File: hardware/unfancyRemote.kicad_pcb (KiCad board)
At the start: 2 copper layers, 27.7 x 59.2 mm, 41 parts, among them J1 Arduino Analog, J2 Arduino Digital, J3 HALL1, J4 HALL2, J5 PPM, J6 VIN, J7 VBAT, J8 Motor, J9 Extra analog 1, Q1 AO3401A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

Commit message: Software v1.0 for rx and tx
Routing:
- net Net-(D6-Pad2): track 0.00 -> 1.99 mm
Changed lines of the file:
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@@
   (segment (start 121.2365 89.662) (end 121.2365 88.2505) (width 0.25) (layer "F.Cu") (net 26))
   (segment (start 121.2365 88.2505) (end 121.603 87.884) (width 0.25) (layer "F.Cu") (net 26))
+  (segment (start 121.603 94.234) (end 121.158 94.679) (width 0.25) (layer "F.Cu") (net 27))
+  (segment (start 121.158 94.679) (end 121.158 95.9335) (width 0.25) (layer "F.Cu") (net 27))
+  (segment (start 121.158 95.9335) (end 121.2365 96.012) (width 0.25) (layer "F.Cu") (net 27))
   (segment (start 123.253 92.057) (end 126.39 88.92) (width 0.25) (layer "F.Cu") (net 28))
   (segment (start 123.253 94.234) (end 123.253 92.057) (width 0.25) (layer "F.Cu") (net 28))

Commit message: Improved transmission stability
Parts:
- added R14: 100K, Resistor_SMD:R_0603_1608Metric, F.Cu at (144.3, 92.7)
- R1: value 220K -> 100K
- moved J7 4.06 mm to (144.3, 89.4)
- moved R12 2.86 mm to (144.3, 86.4)
- moved R13 2.41 mm to (144.3, 83.2)
- turned R1 to 0 degrees
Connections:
- R1 pad 1: BSENSE -> Net-(R1-Pad1)
- R1 pad 2: GND -> BSENSE
- R3 pad 1: BSENSE -> Net-(R1-Pad1)
- SW1 pad 1: BSENSE -> Net-(R1-Pad1)
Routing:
- net Net-(R1-Pad1): track 0.00 -> 23.1 mm, vias 0 -> 2
- net BSENSE: track 28.0 -> 7.62 mm, vias 2 -> 0
- net Net-(J7-Pad1): track 3.43 -> 2.22 mm

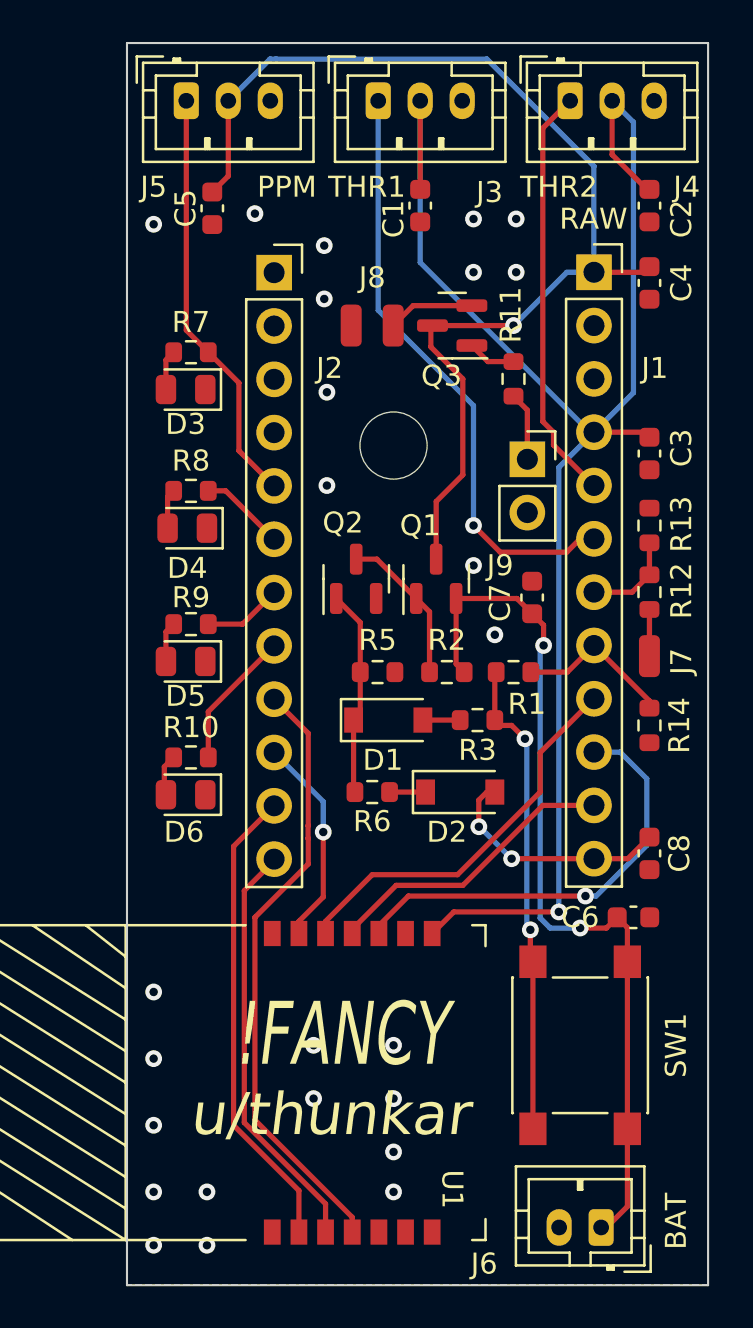
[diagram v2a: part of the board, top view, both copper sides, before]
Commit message: PCB improvements, round version, cal procedure
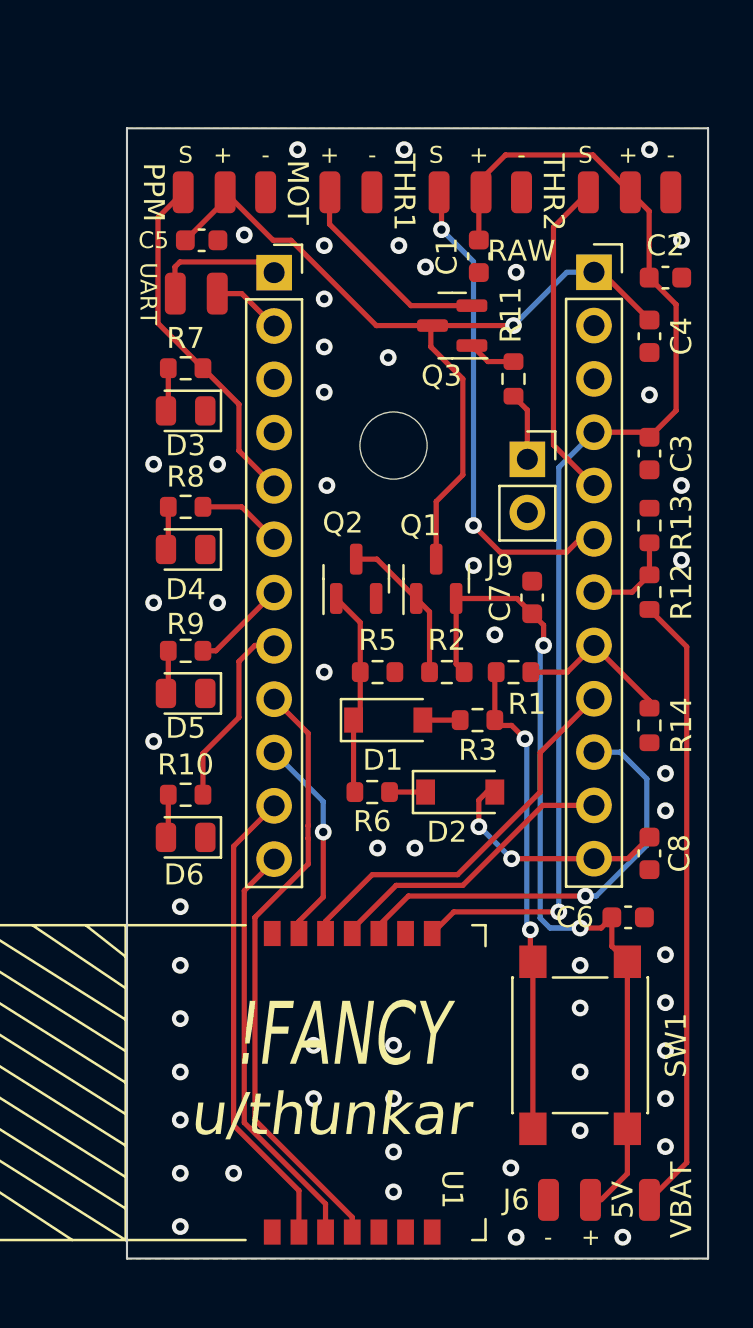
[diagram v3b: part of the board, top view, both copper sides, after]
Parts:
- added J10: UART, unfancyRemote_components:SolderWirePad_1x02_SMD_1x2mm, F.Cu at (122.7, 72.1)
- J3, J4, J5: footprint Connector_JST:JST_PH_B3B-PH-K_1x03_P2.00mm_Vertical -> unfancyRemote_components:SolderWirePad_1x03_SMD_1x2mm
- J6: footprint Connector_JST:JST_PH_B2B-PH-K_1x02_P2.00mm_Vertical -> unfancyRemote_components:SolderWirePad_1x02_SMD_1x2mm
- moved J7 25.9 mm to (144.3, 115.3)
- moved J3 6.48 mm to (136.1, 67.3)
- moved J8 6.43 mm to (130.0, 67.3), turned to 0 degrees
- moved J4 5.16 mm to (143.3, 67.3)
- moved J5 4.70 mm to (124.0, 67.3)
- moved C1 3.69 mm to (136.1, 70.4)
- moved C2 3.51 mm to (145.0, 71.4), turned to 0 degrees
- moved C4 2.54 mm to (144.3, 74.2)
- moved D6 2.03 mm to (122.2, 98.0)
- moved J6 2.00 mm to (140.5, 115.3)
- moved R10 1.80 mm to (122.2, 96.0)
- moved C5 1.61 mm to (122.9, 69.6), turned to 0 degrees
- moved D5 1.52 mm to (122.2, 91.2)
- moved R9 1.30 mm to (122.2, 89.2)
- moved D4 1.02 mm to (122.2, 84.3)
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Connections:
- J2 pad 1: unconnected-(J2-Pad1) -> Net-(J2-Pad1)
- J2 pad 2: unconnected-(J2-Pad2) -> Net-(J2-Pad2)
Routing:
- net Net-(J7-Pad1): track 2.22 -> 29.6 mm
- net +3V3: track 77.5 -> 57.1 mm
- net +5V: track 53.9 -> 40.2 mm
- net Net-(J2-Pad1): track 0.00 -> 6.31 mm
- net Net-(J8-Pad1): track 4.14 -> 9.92 mm
- net HALL1: track 28.6 -> 23.1 mm, vias 1 -> 2
- net HALL2: track 19.9 -> 15.5 mm
- net Net-(J2-Pad2): track 0.00 -> 3.35 mm
- net PPM: track 20.1 -> 16.8 mm
- net L4: track 6.61 -> 9.06 mm
- net 5VRAW: track 42.6 -> 40.9 mm
- net L3: track 3.76 -> 4.54 mm
- net GND: vias 25 -> 55
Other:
- board size 27.7 x 59.2 mm -> 27.7 x 53.8 mm
- board text added: "+"
- board text added: "-"
- board text added: "5V"
- board text added: "MOT"
- board text added: "S"
- board text added: "UART"
- board text added: "VBAT"
- board text removed: "BAT"

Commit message: PCB v2 gerber and bom
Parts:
- moved J9 2.55 mm to (139.0, 82.5), turned to 180 degrees
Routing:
- net MOTOR: track 3.28 -> 6.51 mm
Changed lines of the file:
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@@
   )
   (footprint "Connector_PinSocket_2.54mm:PinSocket_1x02_P2.54mm_Vertical" (layer "F.Cu")
-    (at 138.455 80.03)
+    (at 138.963 82.53 180)
     (descr "Through hole straight socket strip, 1x02, 2.54mm pitch, single row (from Kicad 4.0.7), script generated")
     (tags "Through hole socket strip THT 1x02 2.54mm single row")
@@
     (fp_line (start 1.27 -0.635) (end 1.27 3.81) (layer "F.Fab") (width 0.1))
     (fp_line (start 0.635 -1.27) (end 1.27 -0.635) (layer "F.Fab") (width 0.1))
-    (pad "1" thru_hole rect (at 0 0) (size 1.7 1.7) (drill 1) (layers *.Cu *.Mask)
+    (pad "1" thru_hole rect (at 0 0 180) (size 1.7 1.7) (drill 1) (layers *.Cu *.Mask)
       (net 37 "MOTOR") (pinfunction "A4") (pintype "passive"))
-    (pad "2" thru_hole oval (at 0 2.54) (size 1.7 1.7) (drill 1) (layers *.Cu *.Mask)
+    (pad "2" thru_hole oval (at 0 2.54 180) (size 1.7 1.7) (drill 1) (layers *.Cu *.Mask)
       (net 38 "unconnected-(J9-Pad2)") (pinfunction "A5") (pintype "passive+no_connect"))
     (model "${KICAD6_3DMODEL_DIR}/Connector_PinSocket_2.54mm.3dshapes/PinSocket_1x02_P2.54mm_Vertical.wrl"
@@
   (segment (start 144.259 71.374) (end 144.259 68.207) (width 0.25) (layer "F.Cu") (net 4))
   (via (at 139.954 101.594161) (size 0.8) (drill 0.4) (layers "F.Cu" "B.Cu") (net 4))
-  (segment (start 139.954 80.416) (end 141.63 78.74) (width 0.25) (layer "B.Cu") (net 4))
-  (segment (start 139.954 101.594161) (end 139.954 80.416) (width 0.25) (layer "B.Cu") (net 4))
+  (segment (start 141.63 78.74) (end 140.208 80.162) (width 0.25) (layer "B.Cu") (net 4))
+  (segment (start 140.208 101.340161) (end 139.954 101.594161) (width 0.25) (layer "B.Cu") (net 4))
+  (segment (start 140.208 80.162) (end 140.208 101.340161) (width 0.25) (layer "B.Cu") (net 4))
   (segment (start 131.3815 102.624) (end 131.3815 102.244978) (width 0.25) (layer "F.Cu") (net 5))
   (segment (start 132.788478 100.838) (end 141.224 100.838) (width 0.25) (layer "F.Cu") (net 5))
@@
   (segment (start 128.73125 97.79) (end 128.73125 96.34125) (width 0.25) (layer "B.Cu") (net 17))
   (segment (start 128.73125 96.34125) (end 126.39 94) (width 0.25) (layer "B.Cu") (net 17))
-  (segment (start 139.7 79.35) (end 139.7 68.972) (width 0.25) (layer "F.Cu") (net 18))
-  (segment (start 141.63 81.28) (end 139.7 79.35) (width 0.25) (layer "F.Cu") (net 18))
   (segment (start 139.7 68.972) (end 141.362 67.31) (width 0.25) (layer "F.Cu") (net 18))
+  (segment (start 140.462 79.23301) (end 139.7 78.47101) (width 0.25) (layer "F.Cu") (net 18))
+  (segment (start 139.7 78.47101) (end 139.7 68.972) (width 0.25) (layer "F.Cu") (net 18))
+  (segment (start 141.63 81.28) (end 140.462 80.112) (width 0.25) (layer "F.Cu") (net 18))
+  (segment (start 140.462 80.112) (end 140.462 79.23301) (width 0.25) (layer "F.Cu") (net 18))
   (segment (start 137.16 84.455) (end 135.89 83.185) (width 0.25) (layer "F.Cu") (net 19))
   (segment (start 140.335 84.455) (end 137.16 84.455) (width 0.25) (layer "F.Cu") (net 19))
@@
   (segment (start 135.8115 72.71) (end 132.908 72.71) (width 0.25) (layer "F.Cu") (net 36))
   (segment (start 132.908 72.71) (end 129.032 68.834) (width 0.25) (layer "F.Cu") (net 36))
-  (segment (start 138.455 77.685) (end 137.795 77.025) (width 0.25) (layer "F.Cu") (net 37))
-  (segment (start 138.455 80.03) (end 138.455 77.685) (width 0.25) (layer "F.Cu") (net 37))
+  (segment (start 137.788489 77.031511) (end 137.788489 77.603511) (width 0.25) (layer "F.Cu") (net 37))
+  (segment (start 137.16 80.727) (end 138.963 82.53) (width 0.25) (layer "F.Cu") (net 37))
+  (segment (start 137.795 77.025) (end 137.788489 77.031511) (width 0.25) (layer "F.Cu") (net 37))
+  (segment (start 137.788489 77.603511) (end 137.16 78.232) (width 0.25) (layer "F.Cu") (net 37))
+  (segment (start 137.16 78.232) (end 137.16 80.727) (width 0.25) (layer "F.Cu") (net 37))
   (segment (start 136.5765 75.375) (end 135.8115 74.61) (width 0.25) (layer "F.Cu") (net 39))
   (segment (start 137.795 75.375) (end 136.5765 75.375) (width 0.25) (layer "F.Cu") (net 39))

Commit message: wip
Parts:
- added D3: LED, LED_SMD:LED_0805_2012Metric, F.Cu at (102.2, 77.2)
- added D7: LED, LED_SMD:LED_0805_2012Metric, F.Cu at (102.2, 80.3)
- added D8: LED, LED_SMD:LED_0805_2012Metric, F.Cu at (102.2, 83.3)
- added R15: 470, Resistor_SMD:R_0603_1608Metric, F.Cu at (106.4, 82.0)
- added R4: 470, Resistor_SMD:R_0603_1608Metric, F.Cu at (106.4, 77.0)
- added R7: 470, Resistor_SMD:R_0603_1608Metric, F.Cu at (106.4, 79.5)
- added U2: MCP73871-2AA, Package_DFN_QFN:QFN-20-1EP_4x4mm_P0.5mm_EP2.5x2.5mm, F.Cu at (107.5, 86.4)
- added U3: ESP32-C3_SUPERMINI, unfancyRemote_components:MODULE_ESP32-C3_SUPERMINI, F.Cu at (159.3, 78.0)
- J3: value HALL1 -> HALL1/PPM
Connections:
- J3 pad 1: HALL1 -> HALL1/PPM
- R10 pad 2: L4 -> L1
- R8 pad 2: L2 -> L1
- R9 pad 2: L3 -> L1
- U1 pad 11: /DIO1 -> unconnected-(U1-DIO1-Pad11)

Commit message: power progress
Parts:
- removed  : MountingHole_3.2mm_M3_DIN965, MountingHole:MountingHole_3.2mm_M3_DIN965
- removed C1, C2, C3, C4, C5: 1uF, Capacitor_SMD:C_0603_1608Metric
- removed the D3 at (122.2, 77.7)
- removed J10: UART, unfancyRemote_components:SolderWirePad_1x02_SMD_1x2mm
- removed J2: Arduino Digital, Connector_PinSocket_2.54mm:PinSocket_1x12_P2.54mm_Vertical
- removed J5: PPM, unfancyRemote_components:SolderWirePad_1x03_SMD_1x2mm
- removed J7: VBAT, Connector_wire:SolderWirePad_1x01_SMD_1x2mm
- removed J9: Extra analog 1, Connector_PinSocket_2.54mm:PinSocket_1x02_P2.54mm_Vertical
- removed R10, R8, R9: 220, Resistor_SMD:R_0603_1608Metric
- removed the R7 at (122.2, 75.7)
- added C10: 4.7uF, Capacitor_Tantalum_SMD:CP_EIA-3216-10_Kemet-I, F.Cu at (136.9, 75.7)
- added C11: 10uF, Capacitor_Tantalum_SMD:CP_EIA-3216-10_Kemet-I, F.Cu at (158.2, 108.5)
- added C12: 1uF, Capacitor_SMD:C_0402_1005Metric, F.Cu at (83.0, 77.4)
- added C13: 10uF, Capacitor_Tantalum_SMD:CP_EIA-3216-10_Kemet-I, F.Cu at (129.8, 91.9)
- added C14: 10uF, Capacitor_Tantalum_SMD:CP_EIA-3216-10_Kemet-I, F.Cu at (136.4, 91.9)
- added C15: 1uF, Capacitor_SMD:C_0402_1005Metric, F.Cu at (86.5, 90.2)
- added C16: 100nF, Capacitor_SMD:C_0402_1005Metric, F.Cu at (86.5, 92.2)
- added C9: 4.7uF, Capacitor_Tantalum_SMD:CP_EIA-3216-10_Kemet-I, F.Cu at (128.2, 73.3)
- added D10: WS2812B, LED_SMD:LED_WS2812B-2020_PLCC4_2.0x2.0mm, F.Cu at (98.7, 69.0)
- added D9: D_Schottky, Diode_SMD:D_SOD-523, F.Cu at (89.7, 90.4)
- added L1: 3.3uH, Inductor_SMD:L_01005_0402Metric, F.Cu at (162.3, 99.1)
- added R16: 1K, Resistor_SMD:R_0402_1005Metric, F.Cu at (128.1, 69.3)
- added R17: 10K, Resistor_SMD:R_0402_1005Metric, F.Cu at (128.1, 70.4)
- added R18: 18.2K, Resistor_SMD:R_0402_1005Metric, F.Cu at (83.0, 84.9)
- added R19: 68K, Resistor_SMD:R_0402_1005Metric, F.Cu at (83.0, 87.4)
- added R20: 27K, Resistor_SMD:R_0402_1005Metric, F.Cu at (83.0, 89.9)
- added RT1: 1K, Resistor_SMD:R_0402_1005Metric, F.Cu at (136.1, 69.6)
- added RT2: 150K, Resistor_SMD:R_0402_1005Metric, F.Cu at (136.1, 71.6)
- added TH1: 10K, Resistor_SMD:R_0402_1005Metric, F.Cu at (136.1, 70.6)
- added U4: TPS61085DGK, Package_SO:VSSOP-8_3x3mm_P0.65mm, F.Cu at (137.4, 80.7)
- added U5: MIC5219-3.3YM5, Package_TO_SOT_SMD:SOT-23-5, F.Cu at (133.6, 81.8)
- C6, C8: value 1uF -> 10uF; footprint Capacitor_SMD:C_0603_1608Metric -> Capacitor_Tantalum_SMD:CP_EIA-3216-10_Kemet-I
- C7: value 1uF -> 1.6nF; footprint Capacitor_SMD:C_0603_1608Metric -> Capacitor_SMD:C_0402_1005Metric
- D4, D5, D6: value LED -> WS2812B; footprint LED_SMD:LED_0805_2012Metric -> LED_SMD:LED_WS2812B-2020_PLCC4_2.0x2.0mm
- J1: value Arduino Analog -> Battery; footprint Connector_PinSocket_2.54mm:PinSocket_1x12_P2.54mm_Vertical -> unfancyRemote_components:SolderWirePad_1x02_SMD_1x2mm
- R1, R11, R12, R13, R14, R15, R2, R3, R4, R5, R6, R7: footprint Resistor_SMD:R_0603_1608Metric -> Resistor_SMD:R_0402_1005Metric
- U1, U3: moved to B.Cu
- moved C7 56.9 mm to (83.0, 74.9), turned to 0 degrees
- moved D6 40.2 mm to (98.7, 65.5), turned to 0 degrees
- moved D5 37.5 mm to (98.7, 61.9), turned to 0 degrees
- moved SW1 36.5 mm to (176.3, 117.3)
- moved D4 35.0 mm to (98.7, 58.4), turned to 0 degrees
- moved D7 34.3 mm to (133.7, 66.8), turned to -90 degrees
- moved D8 33.6 mm to (131.4, 66.8), turned to -90 degrees
- moved R14 33.5 mm to (115.3, 109.5)
- moved R15 33.4 mm to (136.6, 67.6), turned to 90 degrees
- moved R4 32.7 mm to (137.7, 67.6), turned to 90 degrees
- moved R7 31.4 mm to (135.5, 67.6), turned to 90 degrees
- moved Q1 29.9 mm to (109.7, 103.0)
- moved R3 29.9 mm to (111.7, 109.7)
- moved R5 29.9 mm to (106.9, 107.4)
- moved D1 29.9 mm to (107.4, 109.7)
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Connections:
- net Net-(U2-OUT-Pad1) renamed VLOAD
- C7 pad 1: 5VRAW -> Net-(C7-Pad1)
- C8 pad 1: ON -> VIN
- D3 pad 2: Net-(D3-A) -> VIN
- D4 pad 1: GND -> Net-(D4-VDD)
- D4 pad 2: Net-(D4-A) -> GND
- D5 pad 1: GND -> Net-(D5-VDD)
- D5 pad 2: Net-(D5-A) -> GND
- D6 pad 1: GND -> Net-(D10-VSS)
- D6 pad 2: Net-(D6-A) -> GND
- D7 pad 2: Net-(D3-A) -> VIN
- D8 pad 2: Net-(D3-A) -> VIN
- J1 pad 1: +5V -> VBAT
- R12 pad 1: Net-(J7-Pin_1) -> VBAT
- U2 pad 12: unconnected-(U2-PROG3-Pad12) -> Net-(U2-PROG3)
- U2 pad 13: unconnected-(U2-PROG1-Pad13) -> Net-(U2-PROG1)
- U2 pad 14: Net-(U2-V_{BAT}-Pad14) -> VBAT
- U2 pad 15: Net-(U2-V_{BAT}-Pad14) -> VBAT
- U2 pad 16: unconnected-(U2-V_{BAT_SENSE}-Pad16) -> VBAT
- U2 pad 17: unconnected-(U2-CE-Pad17) -> VIN
- U2 pad 18: Net-(D3-A) -> VIN
- U2 pad 19: Net-(D3-A) -> VIN
- U2 pad 2: unconnected-(U2-VPCC-Pad2) -> VIN
- U2 pad 3: unconnected-(U2-SEL-Pad3) -> VIN
- U2 pad 4: unconnected-(U2-PROG2-Pad4) -> VIN
- U2 pad 5: unconnected-(U2-THERM-Pad5) -> Net-(U2-THERM)
- U2 pad 9: unconnected-(U2-~{TE}-Pad9) -> VIN
- U3 pad 5V: +5V -> VIN
- U3 pad 8: L1 -> LED
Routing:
- net +3V3: track 57.1 -> 0.00 mm, vias 1 -> 0
- net +5V: track 40.2 -> 0.00 mm, vias 1 -> 0
- net 5VRAW: track 40.9 -> 3.67 mm, vias 2 -> 0
- net Net-(J7-Pin_1): track 29.6 -> 0.00 mm
- net /DIO1: track 29.0 -> 0.00 mm
- net HALL1: track 23.1 -> 0.00 mm, vias 2 -> 0
- net /NRESET: track 22.4 -> 0.00 mm
- net /MISO: track 20.9 -> 0.00 mm, vias 1 -> 0
- net Net-(R1-Pad1): track 23.1 -> 2.31 mm, vias 2 -> 0
- net /RFBUSY: track 20.0 -> 0.00 mm
- net /SCK: track 18.9 -> 0.00 mm
- net PPM: track 16.8 -> 0.00 mm
- net HALL2: track 15.5 -> 0.00 mm
- net /MOSI: track 14.2 -> 0.00 mm
- net ON: track 11.4 -> 0.00 mm, vias 2 -> 0
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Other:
- board size 27.7 x 53.8 mm -> 19.3 x 41.7 mm
- board text removed: "S"
- board text removed: "UART"

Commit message: routing
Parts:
- L1: footprint Inductor_SMD:L_01005_0402Metric -> Inductor_SMD_Wurth:L_Wurth_WE-LQSH-3012
- moved R20 56.6 mm to (138.2, 77.1)
- moved R19 56.0 mm to (138.6, 80.8), turned to -90 degrees
- moved R18 55.9 mm to (138.6, 78.8), turned to -90 degrees
- moved C7 53.2 mm to (136.2, 77.1), turned to 180 degrees
- moved SW1 51.8 mm to (129.5, 95.2)
- moved J6 50.6 mm to (122.9, 89.9), turned to -90 degrees
- moved C12 49.8 mm to (132.8, 78.2)
- moved D9 48.6 mm to (138.1, 85.7), turned to 180 degrees
- moved C16 47.7 mm to (134.0, 88.3), turned to 180 degrees
- moved D4 47.6 mm to (143.2, 75.3), turned to -90 degrees
- moved D5 45.7 mm to (143.2, 72.2), turned to -90 degrees
- moved D6 44.7 mm to (143.2, 69.1), turned to -90 degrees
- moved D10 44.7 mm to (143.2, 66.0), turned to -90 degrees
- moved C15 44.4 mm to (130.8, 87.0), turned to 180 degrees
- moved L1 34.3 mm to (132.4, 82.3), turned to -90 degrees
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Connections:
- U3 pad 0: HALL1 -> HALL1/PPM
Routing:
- net /NRESET: track 0.00 -> 42.6 mm, vias 0 -> 2
- net /RFBUSY: track 0.00 -> 37.4 mm, vias 0 -> 2
- net /SCK: track 0.00 -> 33.7 mm
- net /MISO: track 0.00 -> 32.8 mm
- net /MOSI: track 0.00 -> 30.4 mm, vias 0 -> 2
- net /NSS: track 0.00 -> 29.0 mm, vias 0 -> 2
- net VIN: track 0.00 -> 20.4 mm
- net Net-(D1-K): track 9.40 -> 0.00 mm
- net Net-(U2-~{PG}): track 0.00 -> 5.48 mm
- net Net-(U2-STAT2): track 0.00 -> 5.21 mm
- net VLOAD: track 0.00 -> 4.79 mm
- net Net-(U2-STAT1/~{LBO}): track 0.00 -> 4.72 mm
- net Net-(Q1-G): track 3.77 -> 0.00 mm
- net 5VRAW: track 3.67 -> 0.00 mm
- net VBAT: track 0.00 -> 3.00 mm
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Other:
- board size 19.3 x 41.7 mm -> 23.5 x 41.6 mm
